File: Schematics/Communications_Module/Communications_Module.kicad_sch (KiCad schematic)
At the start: 29 parts, among them SW1 Boot Mode, U1 LMR51430XDDCR, U2 STM32F103CBTx, U3 TMCS1108A3UQDR, U4 ISO1042BQDWVQ1, Y1 16MHz

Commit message: Getting close to a rough schematic
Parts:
- added AE1: Antenna, symbol Device:Antenna
- added C5, C8: C, symbol Device:C
- added J1: USB_B_Micro, symbol Connector:USB_B_Micro
- added R1: 10k, symbol Device:R_US
- added R2: 1.5k, symbol Device:R_US
- added R6: 121, symbol Device:R_US
- added R7: 200, symbol Device:R_US
- added U1: RFM95W-915S2, symbol RF_Module:RFM95W-915S2
- added U2: W25Q128JVPIQ, symbol QRET_Buck_PSU:W25Q128JVPIQ
- added U4: LM1086CT-3.3/NOPB, symbol QRET_Buck_PSU:LM1086CT-3.3_NOPB
- renumbered C1 to C10, C2 to C11, C4 to C12, C7 to C13, C9 to C14, C10 to C16, C12 to C17, C14 to C18, C3 to C6, C6 to C7, C15 to C9, R1 to R3, U1 to U3, U2 to U5, U3 to U6, U4 to U7
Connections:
- net GND1 is gone; now on net +3.3V: C2.1, U7.4 (GND1)
- net +3.3V: now also C2.2, U7.1 (VCC1), C5.2, C8.2, J1.5 (GND), R1.1, R2.1, R7.2, U1.1 (GND), U1.10 (GND), U1.13 (3.3V), U1.8 (GND), U2.8 (VCC)
- net Vsense: now also U5.11 (PA1); no longer U6.7 (VOUT)
- net Vusb: now also C5.1, J1.1 (VBUS), U4.3 (INPUT)
- net Isense: now reaches U5.10 (PA0)
- net Isense: now also U6.7 (VOUT)
- net RESET_RF: now reaches U5.13 (PA3)
- net RESET_RF: now also R1.2, U1.6 (RESET)
- net NSS_RF: now reaches U5.14 (PA4)
- net NSS_RF: now also U1.5 (NSS)
- net SCK_RF: now reaches U5.15 (PA5)
- net SCK_RF: now also U1.4 (SCK)
- net MISO_RF: now reaches U5.16 (PA6)
- net MISO_RF: now also U1.2 (MISO)
- net MOSI_RF: now reaches U5.17 (PA7)
- net MOSI_RF: now also U1.3 (MOSI)
- net D-: now reaches U5.32 (PA11)
- net D-: now also J1.2 (D-)
- net D+: now reaches U5.33 (PA12)
- net D+: now also J1.3 (D+), R2.2
- net CAN_RX: now reaches U5.45 (PB8)
- net CAN_RX: now also U7.3 (RXD)
- net CAN_TX: now reaches U5.46 (PB9)
- net CAN_TX: now also U7.2 (TXD)
- new net: R6.2, R7.1, U4.1 (ADJ)
- new net: AE1.1 (A), U1.9 (ANT)
- new net Vlinreg: C8.1, R6.1, U4.2 (OUTPUT)
- no-connect marks 1 -> 4
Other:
- note added: "-> go to connectors ->"
- note added: "Also SPI no ic2 Compatible with multiple SPI modes, best?"
- note added: "Buzzer"
- note added: "Current Sense"
- note added: "Decoupling cap has to be atleast 4.7uF. Best value? Most designs use two 4.7's in series? (~2.2uF seen)"
- note added: "Flash Module"
- note added: "Ideal diodes right?"
- note added: "Need battery measurement"
- note added: "Need buzzer"
- note added: "Need iso GND, and iso power supply VCC2 range: 4.5 > VCC2 > 5.5"
- note added: "No ic2 uses SPI instead"
- note added: "Prob want LEDS"
- note added: "RF"
- note added: "Recommended around 1% accuracy for resistors, Look into R values more cause current"
- note added: "Reverse polarity protection?"
- note added: "Stack Edge Connector"
- note added: "Vo= 1.25 (1 + R2 / R1) 3.3 = 1.25 (1 + R2 / 121) => R2 = 198.44 = ~200"
- note added: "need to look over data sheet on what these do and what we need"
- note removed: "--->"
- note removed: "Can use resistors on EN to have UVLO if wanted?"
- note removed: "Current Sense?"
- note removed: "Decoupling cap has to be atleast 4.7uF. Best value? Most designs use two 4.7's in series (~2.2uF seen)"
- note removed: "Need two isolated grounds? Isolated power supply?"
- note removed: "USB + Linear Regulation"
- moved on the sheet: C1, C10, C11, C12, C13, C14, C16, C17, C18, C2, C3, C4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

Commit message: Sourced datasheets, symbols, and footprints for all parts on list. Added all relevant symbols to schematic for the most part.
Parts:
- removed C5, C8: C, symbol Device:C
- removed C5: 0.1u, symbol Device:C
- removed C7: 10p, symbol Device:C
- removed R6: 121, symbol Device:R_US
- removed R7: 200, symbol Device:R_US
- removed U2: W25Q128JVPIQ, symbol QRET_Buck_PSU:W25Q128JVPIQ
- removed U4: LM1086CT-3.3/NOPB, symbol QRET_Buck_PSU:LM1086CT-3.3_NOPB
- removed U6: TMCS1108A3UQDR, symbol QRET_Buck_PSU:TMCS1108A3UQDR
- added C5: 26p, symbol Device:C
- added J2: Bus_PCI_Express_x1, Connector_PCBEdge:BUS_PCIexpress_x1, symbol Connector:Bus_PCI_Express_x1
- added U10: PKM13EPYH4000-A0, symbol QRET_Buck_PSU:PKM13EPYH4000-A0
- added U2: W25Q128JVSIQ, SOIC_128JVSIQ_WIN, symbol QRET_Buck_PSU:W25Q128JVSIQ
- added U4, U9: LM66100DCKR, DCK6_TEX, symbol QRET_Buck_PSU:LM66100DCKR
- added U6: ACS70331EOLCTR-2P5U3, SOIC127P600X175-8N, symbol QRET_Buck_PSU:ACS70331EOLCTR-2P5U3
- added U8: AMS1117-3.3, Package_TO_SOT_SMD:SOT-223-3_TabPin2, symbol Regulator_Linear:AMS1117-3.3
- C6: value 10p -> 26p
- Y1: value 16MHz -> X322516MMB4SI
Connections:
- net +3.3V: now also C5.2, U2.8 (VCC)
- net OSC_IN: now also C5.1; no longer C6.1
- net OSC_OUT: now also C6.1
- net Vlinreg: now also U8.2 (VO)
- net Vusb: now also U8.3 (VI)
- net Isense renamed V_Isense
- new net: J2.A10 (+3.3V), J2.A9 (+3.3V), J2.B8 (+3.3V)
- new net: J2.A12 (GND), J2.A15 (GND), J2.A18 (GND), J2.A4 (GND), J2.B13 (GND), J2.B16 (GND), J2.B18 (GND), J2.B4 (GND), J2.B7 (GND)
- new net: J2.A2 (+12V), J2.A3 (+12V), J2.B1 (+12V), J2.B2 (+12V), J2.B3 (+12V)
- no-connect marks 4 -> 2
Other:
- note added: "CL=((CL1*CL2)/(CL1_CL2))+ CS CL=20 or 10 pf (datasheet), choose 20 20=((CL1*CL2)/(CL1_CL2))+ CS C shunt = 7pf max (datasheet) CL1=CL2=C 20-7=C^2/2C C=26pf"
- note added: "Going on power board instead"
- note added: "Power"
- note removed: "Buck Regulator"
- note removed: "CL = (CLcrystal - Cstray)* 2 YXC XL7EL89CKI-111YLC-16M Crystal"
- note removed: "Ferrite bead ok?"
- note removed: "Ideal diodes right?"
- note removed: "Need battery measurement"
- note removed: "Need buzzer"
- note removed: "Recommended around 1% accuracy for resistors, Look into R values more cause current"
- note removed: "Vo= 1.25 (1 + R2 / R1) 3.3 = 1.25 (1 + R2 / 121) => R2 = 198.44 = ~200"
- moved on the sheet: C1, C2, C3, C4, J1, L1, R1, R2, U3

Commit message: Rough draft minus things I need to ask about
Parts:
- added C14: 0.1u, symbol Device:C
- added C5, C6: 10u, symbol Device:C
- renumbered C14 to C15, C5 to C7, C6 to C8, R1 to R3, R2 to R4, R3 to R5, U3 to U1, U7 to U10, U8 to U2, U1 to U3, U2 to U4, U10 to U5, U9 to U6, U4 to U7, U6 to U8, U5 to U9
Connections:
- net Vlinreg is gone; now on net Vusb_reg: U2.2 (VO)
- net +3.3V: now also J2.A12 (GND), J2.A15 (GND), J2.A18 (GND), J2.A4 (GND), J2.B13 (GND), J2.B16 (GND), J2.B18 (GND), J2.B4 (GND), J2.B7 (GND), U2.1 (GND), U4.4 (GND), U6.2 (GND), U7.2 (GND), U8.3 (IP-_1), U8.4 (IP-_2), U8.5 (GND), U8.8 (VCC), C14.1, C14.2, C5.2, C6.2
- net V_Isense: now also U8.7 (VIOUT)
- net Vo,OR: now also U6.6 (VOUT), U7.6 (VOUT), U8.1 (IP+_1), U8.2 (IP+_2)
- net Vusb: now also C5.1
- net Vusb_reg: now reaches U7.1 (VIN)
- net Vusb_reg: now also U6.3 (*CE), C6.1
- net Vpsu: now reaches U7.3 (*CE)
- net Vpsu: now also U6.1 (VIN)
- no-connect marks 2 -> 5
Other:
- note added: "Caps for stability needed?"
- note added: "Current Sense + 3.3V output"
- note added: "Need to know what SPI mode"
- note added: "Power ORing"
- note added: "ST pins are just status indication, Want a way to keep track of what power supply active?"
- note added: "USB"
- note added: "Vout"
- note added: "fixed AMS1117?"
- note added: "idk if this the right symbol, or much about connectors tbh"
- note removed: "Current Sense"
- note removed: "Power"
- moved on the sheet: J1, R4, U2, U6, U7, U8

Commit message: Added last few sub-circuits (buzzer, SWD), connected a bunch of pins between modules and STM, changed ideal diode circuit. Overall, rough draft minus edge connector
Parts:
- removed C2, C3: 0.1u, symbol Device:C
- removed C4: C, symbol Device:C
- removed L1: L, symbol Device:L
- removed R2: 22k, symbol Device:R_US
- removed U1: LMR51430XDDCR, symbol QRET_Buck_PSU:LMR51430XDDCR
- removed U4: W25Q128JVSIQ, SOIC_128JVSIQ_WIN, symbol QRET_Buck_PSU:W25Q128JVSIQ
- removed U5: PKM13EPYH4000-A0, symbol QRET_Buck_PSU:PKM13EPYH4000-A0
- removed U7: LM66100DCKR, DCK6_TEX, symbol QRET_Buck_PSU:LM66100DCKR
- removed U8: ACS70331EOLCTR-2P5U3, SOIC127P600X175-8N, symbol QRET_Buck_PSU:ACS70331EOLCTR-2P5U3
- added BZ1: PKM13EPYH4000-A0, symbol Device:Buzzer
- added C15: 1000u, symbol Device:C
- added C5, C6, C8: 1u, symbol Device:C
- added J3: Conn_01x04_Pin, symbol Connector:Conn_01x04_Pin
- added Q1: NMOS, symbol Simulation_SPICE:NMOS
- added R3, R5: 10k, symbol Device:R_US
- added R4: 500, symbol Device:R_US
- added R6: 1k, symbol Device:R_US
- added U2: W25Q128JVSIQ, symbol Memory_Flash:W25Q128JVS
- added U4, U5: LM66100DCKR, DCK6_TEX, symbol QRET_Buck_PSU:LM66100DCKR
- added U8: ACS706xLC-05C, symbol Sensor_Current:ACS706xLC-05C
- C1: value C -> 100n
- J2: footprint Connector_PCBEdge:BUS_PCIexpress_x1 -> (none)
- R1: value 99k -> 10k
- U3: renamed from U2; footprint Package_TO_SOT_SMD:SOT-223-3_TabPin2 -> (none)
- renumbered C15 to C14, C14 to C16, C16 to C17, C17 to C18, C18 to C19, C5 to C2, C6 to C3, C7 to C4, C8 to C7, R3 to R2, R5 to R7, R4 to R8, U3 to U1, U9 to U7, U10 to U9
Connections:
- net Vbatt is gone; now on net +3.3V: C1.1
- net Vbuck is gone; now on net +3.3V: R1.1
- net +3.3V: now also C15.2, C5.2, C6.2, C8.2, J3.1 (Pin_1), Q1.3 (S), R3.1, R5.2, U2.4 (GND), U2.8 (VCC), U4.2 (GND), U5.2 (GND), U8.3 (IP-), U8.4 (IP-), U8.5 (GND); no longer C16.1
- net V_Isense: now also U8.7 (VOUT)
- net CS_FL: now reaches U7.25 (PB12)
- net CS_FL: now also U2.1 (~{CS})
- net SCK_FL: now reaches U7.26 (PB13)
- net SCK_FL: now also U2.6 (CLK)
- net MISO_FL: now reaches U7.27 (PB14)
- net MISO_FL: now also U2.2 (DO(IO1))
- net MOSI_FL: now reaches U7.28 (PB15)
- net MOSI_FL: now also U2.5 (DI(IO0))
- net RESET_FL: now reaches U7.29 (PA8)
- net RESET_FL: now also R1.2, U2.7 (IO3)
- net V_BUZZ: now reaches U7.30 (PA9)
- net V_BUZZ: now also R4.1
- net SWDIO: now reaches U7.34 (PA13)
- net SWDIO: now also J3.3 (Pin_3)
- net SDCLK: now reaches U7.37 (PA14)
- net DIO0_RF: now reaches U1.14 (DIO0)
- net DIO2_RF: now reaches U1.16 (DIO2)
- net DIO5_RF: now reaches U1.7 (DIO5)
- net Vo,OR renamed V_DIODE
- net V_DIODE: now also C16.1, U6.3 (*CE), C15.1, U4.3 (*CE), U4.6 (VOUT), U5.3 (*CE), U5.6 (VOUT), U8.1 (IP+), U8.2 (IP+), U8.8 (VCC)
- net Vpsu renamed V_SWD
- net V_SWD: now also C6.1, J3.4 (Pin_4)
- net Vusb renamed V_USB
- net Vusb_reg renamed V_REGUSB
- net V_REGUSB: now also C8.1, U5.1 (VIN); no longer U6.3 (*CE)
- new net: R3.2, U2.3 (IO2)
- new net: Q1.2 (G), R4.2, R5.1
- new net: BZ1.2 (+), Q1.1 (D), R6.2
- new net: BZ1.1 (-), R6.1
- new net SWCLK: J3.2 (Pin_2)
- new net V_PSU: C5.1, U4.1 (VIN)
- no-connect marks 5 -> 2
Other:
- note added: "Also SPI no ic2"
- note added: "Ideal Diodes"
- note added: "Maybe put V_Isense and Vsense on PA13/10 to keep then close to USB/Pwr stuff Could make routing easier, fills that side of the chip tho, nvm swd :( PA10/15 ?"
- note added: "Serial Wire Debug"
- note added: "can u use the same pullup?"
- note added: "is this how the voltage from swd works?"
- note added: "need to find applicable STM pins"
- note added: "needed if same node as 1000u"
- note added: "waiting on custom PCi-e sym"
- note added: "what voltage here?"
- note removed: "-->"
- note removed: "Also SPI no ic2 Compatible with multiple SPI modes, best?"
- note removed: "Decoupling cap has to be atleast 4.7uF. Best value? Most designs use two 4.7's in series? (~2.2uF seen)"
- note removed: "Going on power board instead"
- note removed: "Need to know what SPI mode"
- note removed: "Power Mux"
- note removed: "Power ORing"
- note removed: "R2 selected to control current through branch R1 to control Vout (R1 could prob go to 100k) Current in branch , I=V/R=3.3/121k=~27uA"
- note removed: "Reverse polarity protection?"
- note removed: "idk if this the right symbol, or much about connectors tbh"
- moved on the sheet: C16, C2, C3, J1, J2, R8, U3

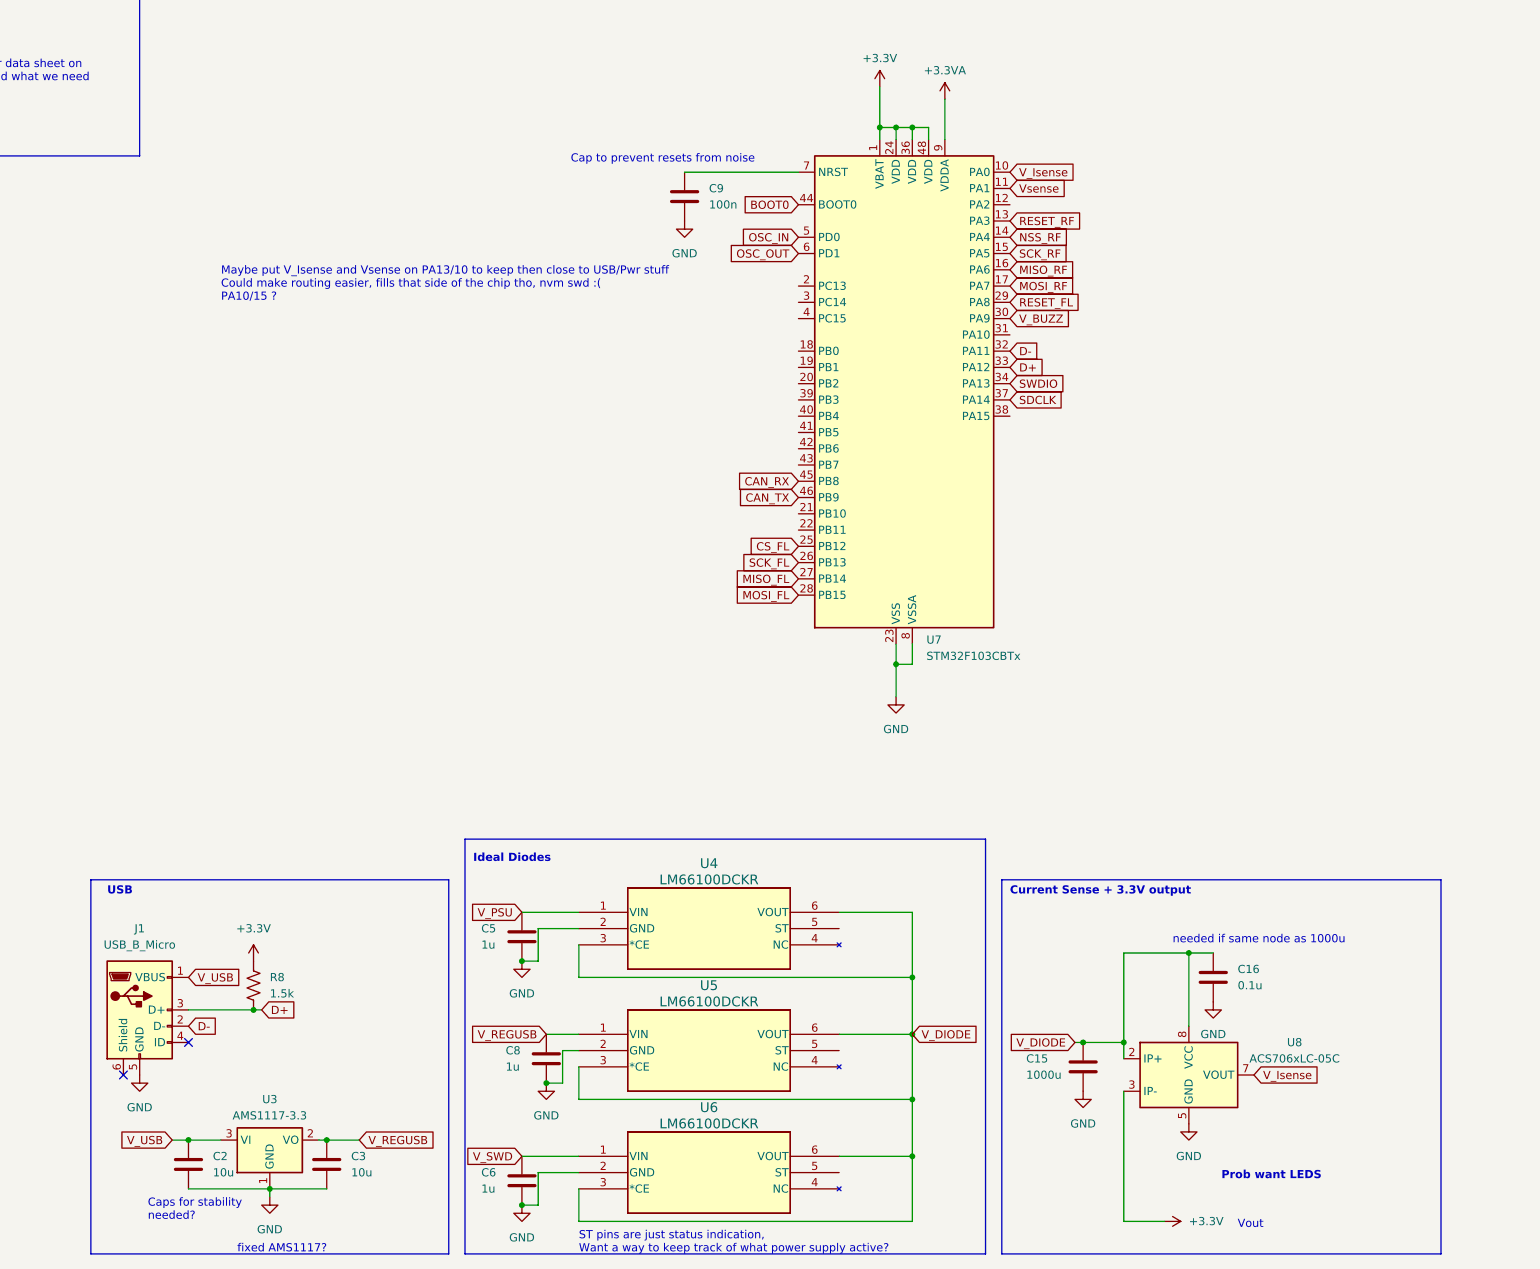
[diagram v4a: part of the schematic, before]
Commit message: Forgot LEDs in last commit so adding them, need a bit more input for RGB tho
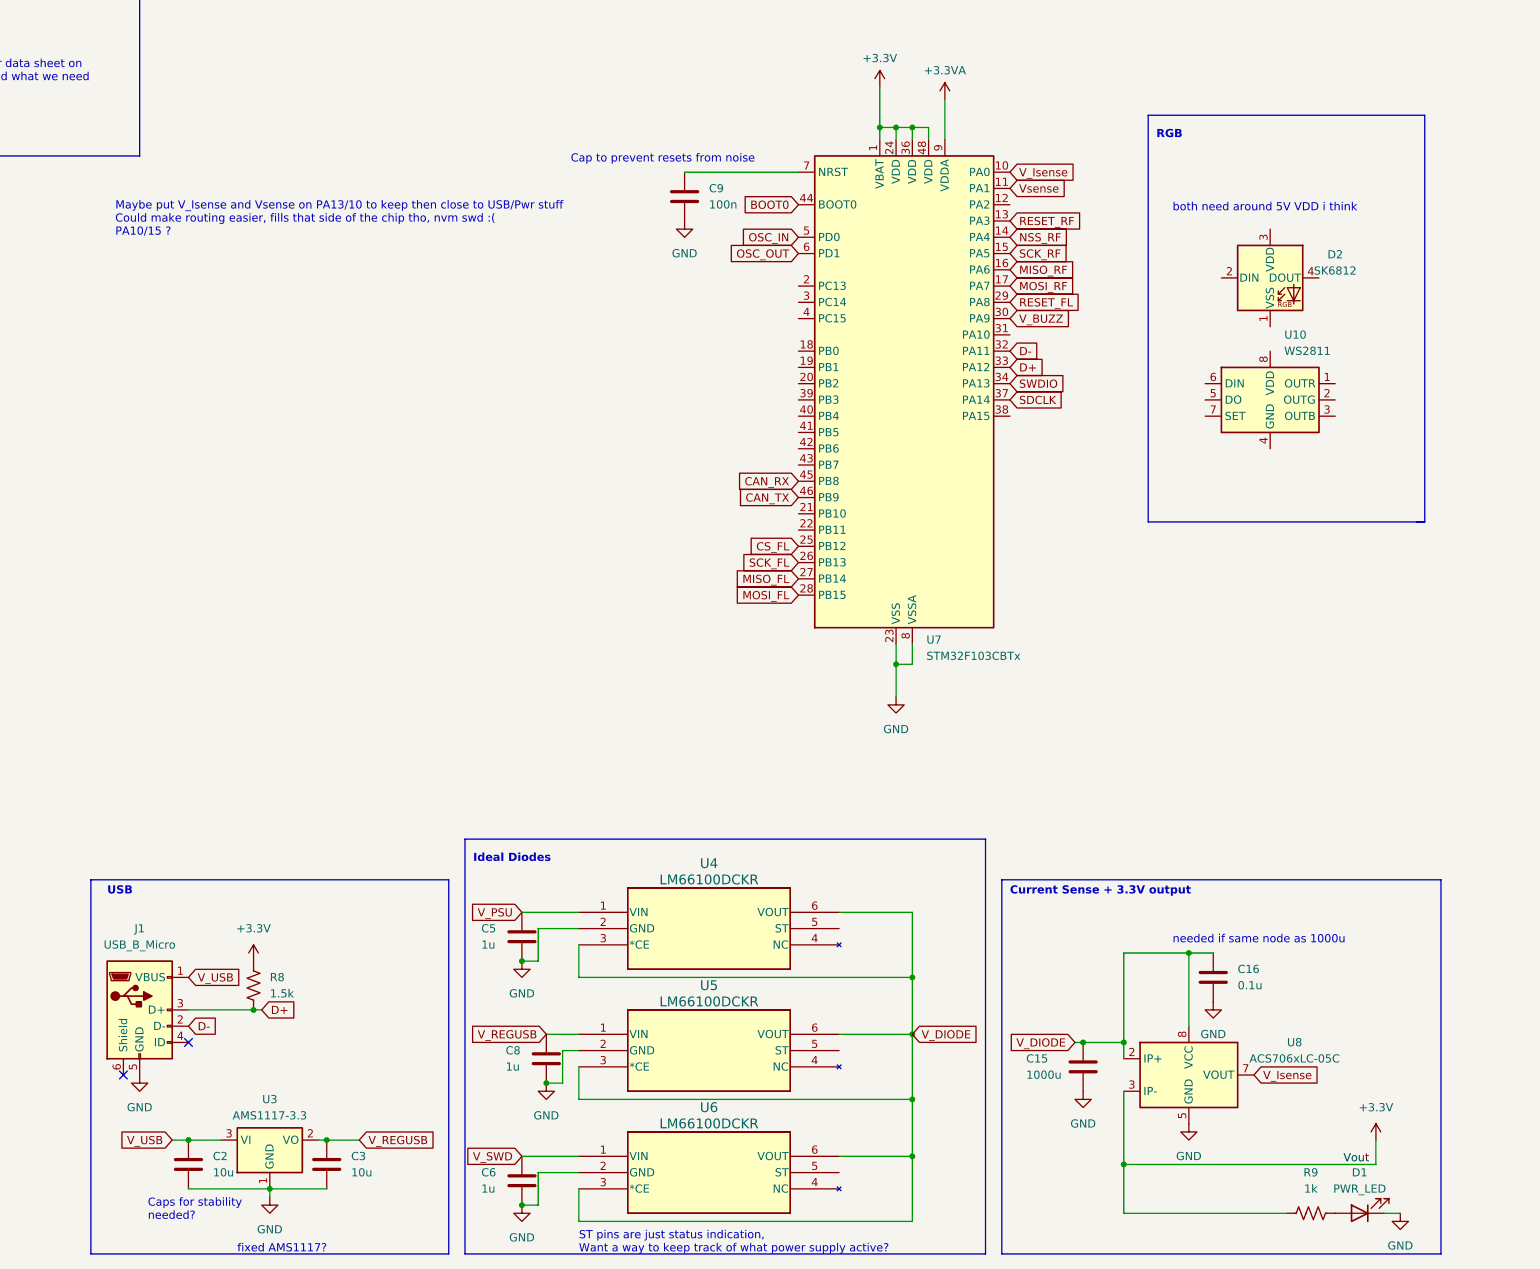
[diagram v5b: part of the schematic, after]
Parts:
- added D1: PWR_LED, symbol Device:LED
- added D2: SK6812, LED_SMD:LED_SK6812_PLCC4_5.0x5.0mm_P3.2mm, symbol LED:SK6812
- added R9: 1k, symbol Device:R_US
- added U10: WS2811, symbol Driver_LED:WS2811
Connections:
- net +3.3V: now also D1.1 (K), R9.1
- new net: D1.2 (A), R9.2
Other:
- note added: "RGB"
- note added: "both need around 5V VDD i think"
- note removed: "Prob want LEDS"
- note removed: "Vout"
